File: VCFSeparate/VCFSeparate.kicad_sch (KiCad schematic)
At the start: 0 parts

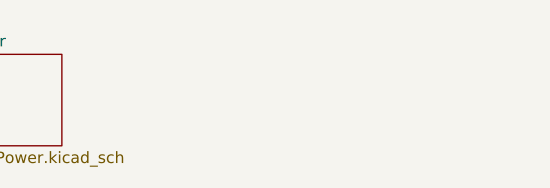
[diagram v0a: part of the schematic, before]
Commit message: MC2
VCO,VCF+VCA,Powerを登録
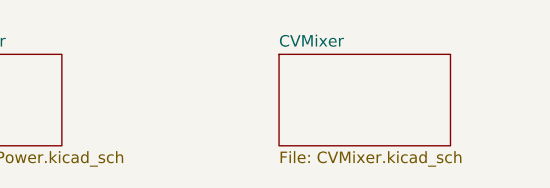
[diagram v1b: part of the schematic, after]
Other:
- added sheet CVMixer (CVMixer.kicad_sch)
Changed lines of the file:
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@@
 	(paper "A4")
+	(sheet
+		(at 142.24 27.94)
+		(size 19.05 10.16)
+		(fields_autoplaced yes)
+		(stroke
+			(width 0.1524)
+			(type solid)
+		)
+		(fill
+			(color 0 0 0 0.0000)
+		)
+		(property "Sheetname" "CVMixer"
+			(at 142.24 27.2284 0)
+			(effects
+				(font
+					(size 1.27 1.27)
+				)
+				(justify left bottom)
+			)
+		)
+		(property "Sheetfile" "CVMixer.kicad_sch"
+			(at 142.24 38.6846 0)
+			(effects
+				(font
+					(size 1.27 1.27)
+				)
+				(justify left top)
+			)
+		)
+		(instances
+			(project "VCFSeparate"
+				(path "/02fc5d1f-a2a3-4ec9-a454-0bdd0b1ddad0"
+					(page "5")
+				)
+			)
+		)
+	)
 	(sheet
 		(at 97.79 27.94)
